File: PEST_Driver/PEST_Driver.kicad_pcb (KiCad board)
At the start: 2 copper layers, 68 x 53.2 mm, 148 parts, among them J1 Conn_01x02, J10 Conn_01x02, J11 Conn_01x02, J12 Conn_01x02, J13 Conn_01x02, J14 Conn_01x02, J15 Conn_01x02, J16 Conn_01x02, J17 Conn_01x02, J2 Conn_01x02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

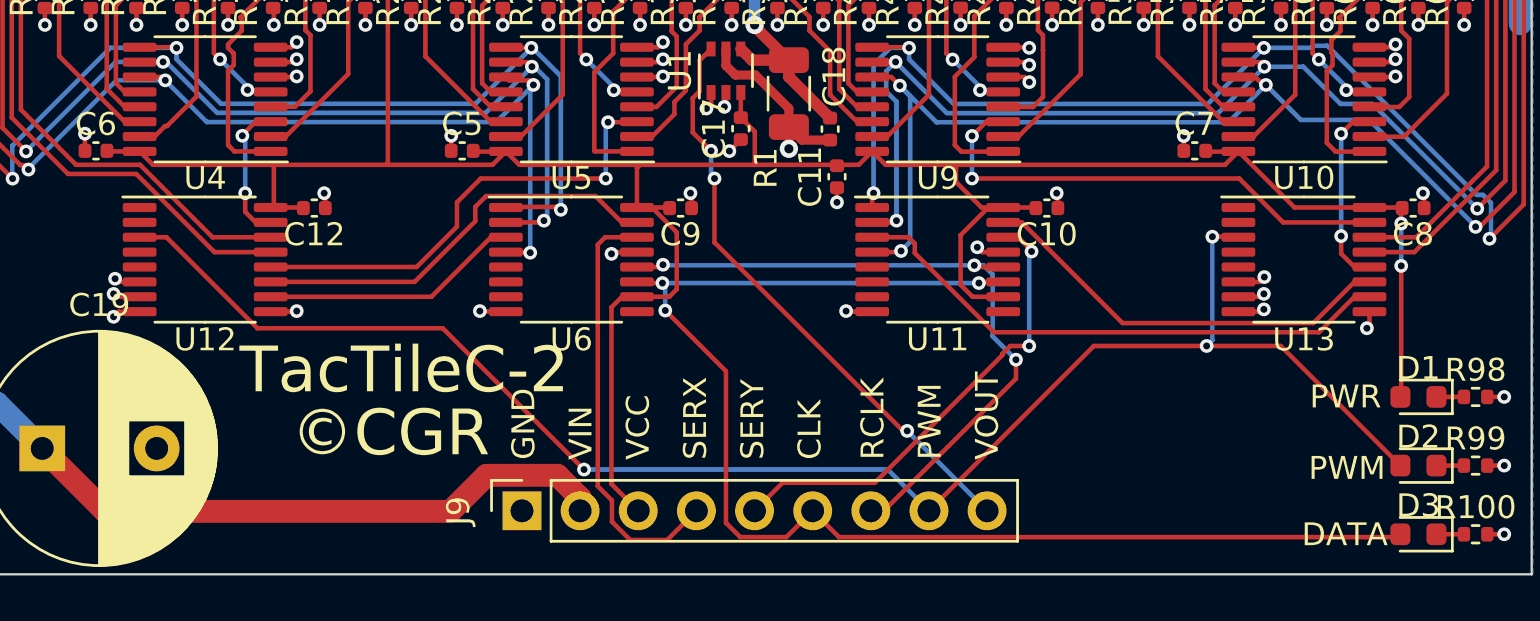
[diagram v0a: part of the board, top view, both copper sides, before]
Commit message: Finished wiring independent MOSFET and logic grounds
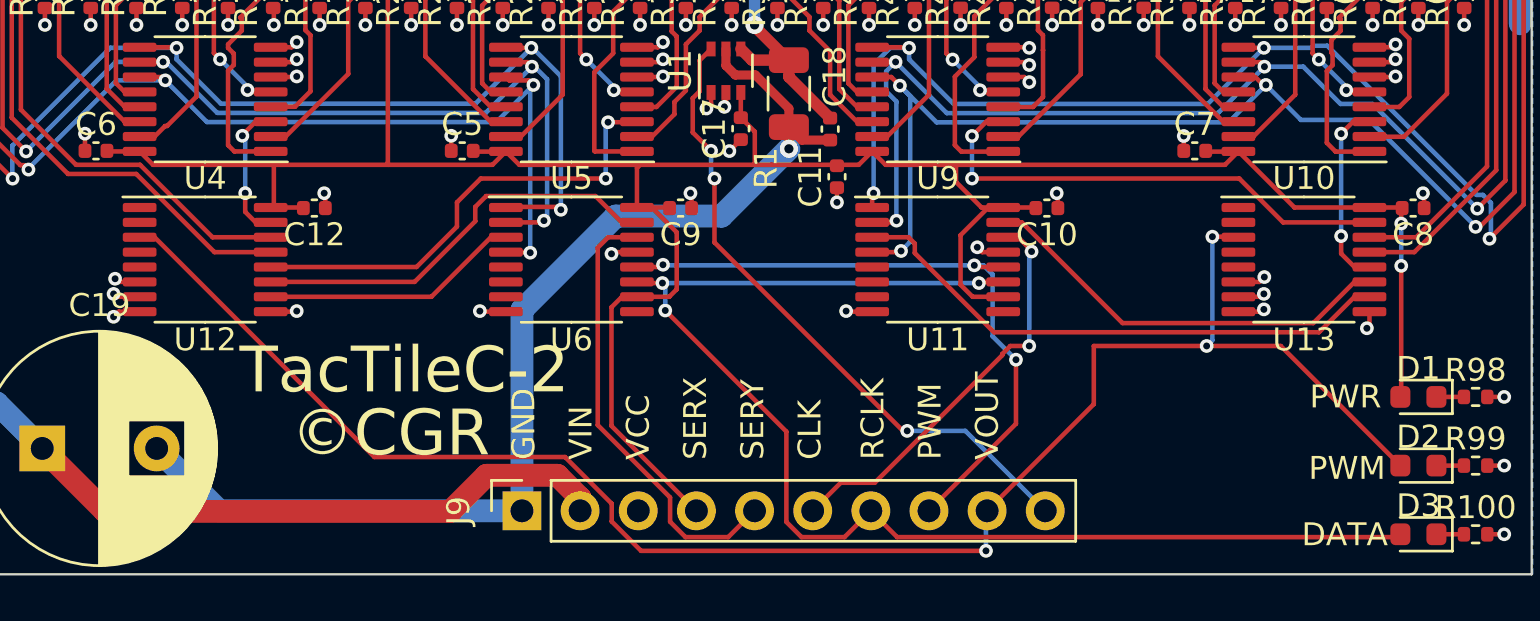
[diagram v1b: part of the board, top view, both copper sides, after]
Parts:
- J9: value Conn_01x09 -> Conn_01x10; footprint Connector_PinSocket_2.54mm:PinSocket_1x09_P2.54mm_Vertical -> Connector_PinSocket_2.54mm:PinSocket_1x10_P2.54mm_Vertical
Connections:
- C1 pad 1: GND -> GNDS
- C10 pad 1: GND -> GNDS
- C11 pad 1: GND -> GNDS
- C12 pad 1: GND -> GNDS
- C17 pad 1: GND -> GNDS
- C2 pad 1: GND -> GNDS
- C3 pad 1: GND -> GNDS
- C4 pad 1: GND -> GNDS
- C5 pad 1: GND -> GNDS
- C6 pad 1: GND -> GNDS
- C7 pad 1: GND -> GNDS
- C8 pad 1: GND -> GNDS
- C9 pad 1: GND -> GNDS
- J9 pad 3: VCC -> GNDS
- J9 pad 4: SERX -> VCC
- J9 pad 5: SERY -> SERX
- J9 pad 6: CLK -> SERY
- J9 pad 7: RCLK -> CLK
- J9 pad 8: PWM -> RCLK
- J9 pad 9: VOUT -> PWM
- R10 pad 1: GND -> GNDS
- R100 pad 2: GND -> GNDS
- R11 pad 2: GND -> GNDS
- R12 pad 1: GND -> GNDS
- R13 pad 2: GND -> GNDS
- R14 pad 1: GND -> GNDS
- R15 pad 2: GND -> GNDS
- R16 pad 1: GND -> GNDS
- R17 pad 2: GND -> GNDS
- R18 pad 1: GND -> GNDS
- R19 pad 2: GND -> GNDS
- R2 pad 1: GND -> GNDS
- R20 pad 1: GND -> GNDS
- R21 pad 2: GND -> GNDS
- R22 pad 1: GND -> GNDS
- R23 pad 2: GND -> GNDS
- R24 pad 1: GND -> GNDS
- R25 pad 2: GND -> GNDS
- R26 pad 1: GND -> GNDS
- R27 pad 2: GND -> GNDS
- R28 pad 1: GND -> GNDS
- R29 pad 2: GND -> GNDS
- R3 pad 2: GND -> GNDS
- R30 pad 1: GND -> GNDS
- R31 pad 2: GND -> GNDS
- R32 pad 1: GND -> GNDS
- R33 pad 2: GND -> GNDS
- R34 pad 1: GND -> GNDS
- R35 pad 2: GND -> GNDS
- R36 pad 1: GND -> GNDS
- R37 pad 2: GND -> GNDS
- R38 pad 1: GND -> GNDS
- R39 pad 2: GND -> GNDS
- R4 pad 1: GND -> GNDS
- R40 pad 1: GND -> GNDS
- R41 pad 2: GND -> GNDS
- R42 pad 1: GND -> GNDS
- R43 pad 2: GND -> GNDS
- R44 pad 1: GND -> GNDS
- R45 pad 2: GND -> GNDS
- R46 pad 1: GND -> GNDS
- R47 pad 2: GND -> GNDS
- R48 pad 1: GND -> GNDS
- R49 pad 2: GND -> GNDS
- R5 pad 2: GND -> GNDS
- R50 pad 1: GND -> GNDS
- R51 pad 2: GND -> GNDS
- R52 pad 1: GND -> GNDS
- R53 pad 2: GND -> GNDS
- R54 pad 1: GND -> GNDS
- R55 pad 2: GND -> GNDS
- R56 pad 1: GND -> GNDS
- R57 pad 2: GND -> GNDS
- R58 pad 1: GND -> GNDS
- R59 pad 2: GND -> GNDS
- R6 pad 1: GND -> GNDS
- R60 pad 1: GND -> GNDS
- R61 pad 2: GND -> GNDS
- R62 pad 1: GND -> GNDS
- R63 pad 2: GND -> GNDS
- R64 pad 1: GND -> GNDS
- R65 pad 2: GND -> GNDS
- R7 pad 2: GND -> GNDS
- R8 pad 1: GND -> GNDS
- R9 pad 2: GND -> GNDS
- R98 pad 2: GND -> GNDS
- R99 pad 2: GND -> GNDS
- U1 pad 1: GND -> GNDS
- U1 pad 2: GND -> GNDS
- U10 pad 6: GND -> GNDS
- U10 pad 7: GND -> GNDS
- U10 pad 8: GND -> GNDS
- U11 pad 13: GND -> GNDS
- U11 pad 8: GND -> GNDS
- U12 pad 6: GND -> GNDS
- U12 pad 7: GND -> GNDS
- U12 pad 8: GND -> GNDS
- U12 pad 9: GND -> GNDS
- U13 pad 6: GND -> GNDS
- U13 pad 7: GND -> GNDS
- U13 pad 8: GND -> GNDS
- U13 pad 9: GND -> GNDS
- U2 pad 6: GND -> GNDS
- U2 pad 7: GND -> GNDS
- U2 pad 8: GND -> GNDS
- U3 pad 6: GND -> GNDS
- U3 pad 7: GND -> GNDS
- U3 pad 8: GND -> GNDS
- U4 pad 6: GND -> GNDS
- U4 pad 7: GND -> GNDS
- U4 pad 8: GND -> GNDS
- U5 pad 6: GND -> GNDS
- U5 pad 7: GND -> GNDS
- U5 pad 8: GND -> GNDS
- U6 pad 13: GND -> GNDS
- U6 pad 8: GND -> GNDS
- U7 pad 6: GND -> GNDS
- U7 pad 7: GND -> GNDS
- U7 pad 8: GND -> GNDS
- U8 pad 6: GND -> GNDS
- U8 pad 7: GND -> GNDS
- U8 pad 8: GND -> GNDS
- U9 pad 6: GND -> GNDS
- U9 pad 7: GND -> GNDS
- U9 pad 8: GND -> GNDS
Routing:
- net GNDS: track 0.00 -> 124.6 mm, vias 0 -> 118
- net GND: track 132.7 -> 48.5 mm, vias 119 -> 1
- net PWM: track 71.2 -> 75.6 mm
- net VOUT: track 25.9 -> 28.5 mm
- net SERY: track 20.7 -> 18.2 mm
- net CLK: track 58.4 -> 56.8 mm
- net RCLK: track 30.8 -> 29.4 mm
- net VCC: track 195.2 -> 196.3 mm
- net SERX: track 18.8 -> 19.6 mm
- added copper zone on B.Cu, net GNDS
- removed copper zone on B.Cu, net GND

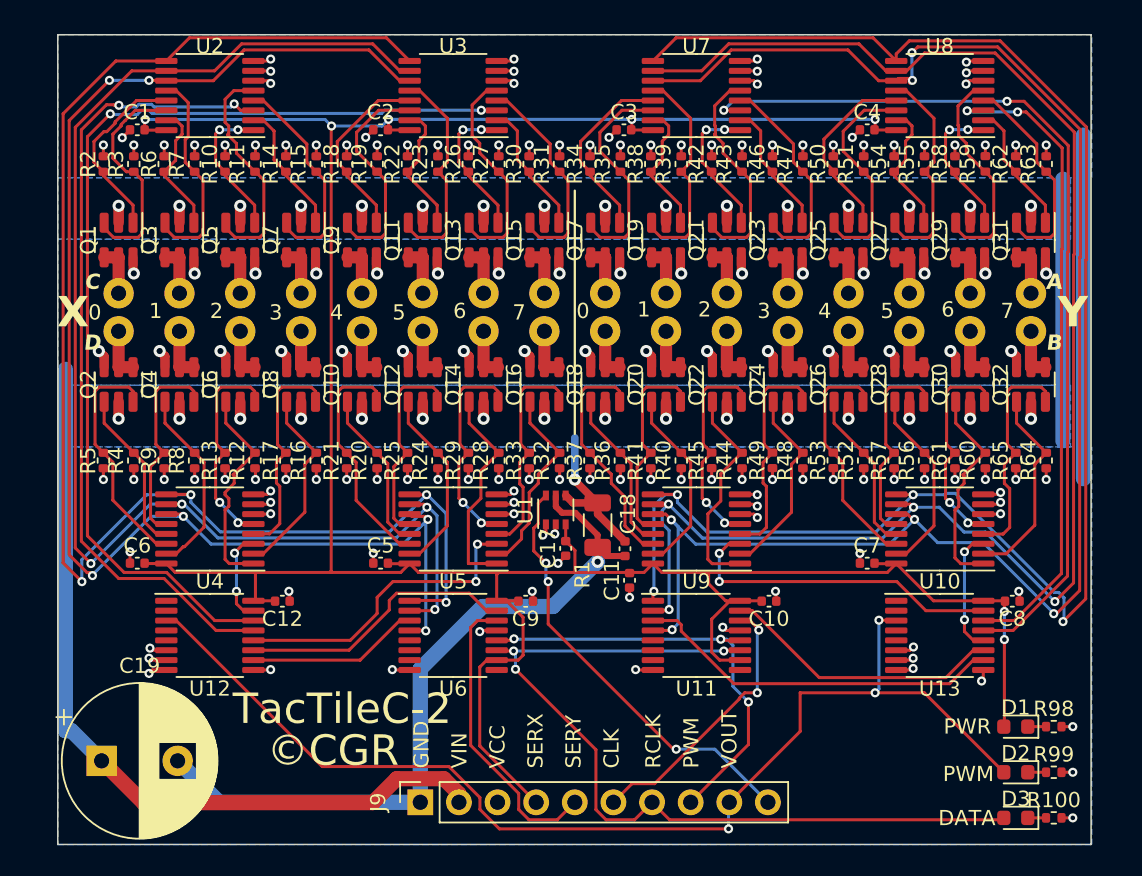
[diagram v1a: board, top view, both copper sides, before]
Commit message: Widened all power traces for more current support
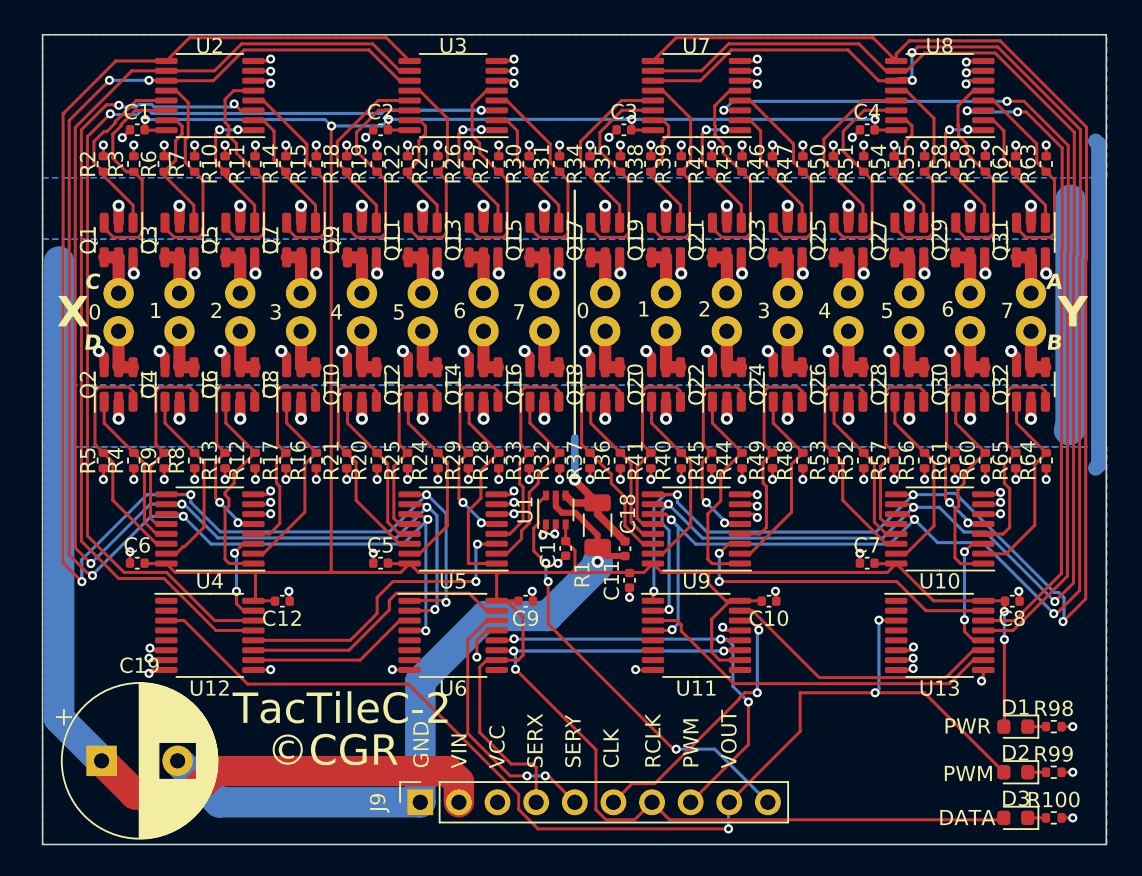
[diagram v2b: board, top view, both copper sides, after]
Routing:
- net VIN: track 89.9 -> 97.3 mm
- net SERX: track 19.6 -> 17.5 mm, vias 0 -> 2
- net SENSE: track 63.3 -> 61.3 mm
- net VCC: track 196.3 -> 197.1 mm
- net GNDS: track 124.6 -> 125.2 mm
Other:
- board size 68 x 53.2 mm -> 70 x 53.2 mm

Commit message: Added more pulldown resistors to PEST Driver
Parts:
- added G***: LOGO, Touchstone:logo, B.Cu at (53.8, 55.1)
- added R66: 10K, Resistor_SMD:R_0402_1005Metric, F.Cu at (66.5, 67.2)
- added R67: 10K, Resistor_SMD:R_0402_1005Metric, F.Cu at (34.8, 59.2)
- added R68: 10K, Resistor_SMD:R_0402_1005Metric, F.Cu at (37.9, 59.2)
- added R69: 10K, Resistor_SMD:R_0402_1005Metric, F.Cu at (37.9, 57.2)
- added R70: 10K, Resistor_SMD:R_0402_1005Metric, F.Cu at (41.0, 56.5)
- added R71: 10K, Resistor_SMD:R_0402_1005Metric, F.Cu at (83.4, 59.2)
- added R72: 10K, Resistor_SMD:R_0402_1005Metric, F.Cu at (85.3, 53.7)
- added R73: 10K, Resistor_SMD:R_0402_1005Metric, F.Cu at (70.0, 56.5)
- added R74: 10K, Resistor_SMD:R_0402_1005Metric, F.Cu at (83.4, 60.9)
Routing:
- net GNDS: track 125.2 -> 131.5 mm, vias 118 -> 127
- net Net-(U12-A1): track 67.3 -> 72.2 mm
- net Net-(U12-A2): track 6.19 -> 11.0 mm
- net Net-(U10-A): track 8.17 -> 10.6 mm
- net Net-(U12-A0): track 53.3 -> 54.7 mm
- net PWM: track 75.7 -> 74.4 mm
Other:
- board text added: "10"
- board text added: "11"
- board text added: "12"
- board text added: "13"
- board text added: "14"
- board text added: "15"
- board text added: "8"
- board text added: "9"
- board text added: "PEST Driver 1.1"
- board text removed: "A"
- board text removed: "B"
- board text removed: "C"
- board text removed: "D"
- board text removed: "TacTileC-2"

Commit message: Created basic DRIFT bus schematic and fixed PEST driver numbering
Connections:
- U10 pad 10: /Y_Control/S0 -> /Y_Control/S1
- U10 pad 9: /Y_Control/S1 -> /Y_Control/S2
- U11 pad 1: /Y_Control/S1 -> /Y_Control/S2
- U11 pad 15: /Y_Control/S2 -> /Y_Control/S3
- U11 pad 2: /Y_Control/S0 -> /Y_Control/S1
- U11 pad 3: /Y_Control/PHA -> /Y_Control/S0
- U12 pad 10: /X_Control/PHA -> /X_Control/S0
- U12 pad 11: /X_Control/S2 -> /X_Control/S3
- U13 pad 10: /Y_Control/PHA -> /Y_Control/S0
- U13 pad 11: /Y_Control/S2 -> /Y_Control/S3
- U2 pad 10: /X_Control/S0 -> /X_Control/S1
- U2 pad 9: /X_Control/S1 -> /X_Control/S2
- U3 pad 10: /X_Control/S0 -> /X_Control/S1
- U3 pad 9: /X_Control/S1 -> /X_Control/S2
- U4 pad 10: /X_Control/S0 -> /X_Control/S1
- U4 pad 9: /X_Control/S1 -> /X_Control/S2
- U5 pad 10: /X_Control/S0 -> /X_Control/S1
- U5 pad 9: /X_Control/S1 -> /X_Control/S2
- U6 pad 1: /X_Control/S1 -> /X_Control/S2
- U6 pad 15: /X_Control/S2 -> /X_Control/S3
- U6 pad 2: /X_Control/S0 -> /X_Control/S1
- U6 pad 3: /X_Control/PHA -> /X_Control/S0
- U7 pad 10: /Y_Control/S0 -> /Y_Control/S1
- U7 pad 9: /Y_Control/S1 -> /Y_Control/S2
- U8 pad 10: /Y_Control/S0 -> /Y_Control/S1
- U8 pad 9: /Y_Control/S1 -> /Y_Control/S2
- U9 pad 10: /Y_Control/S0 -> /Y_Control/S1
- U9 pad 9: /Y_Control/S1 -> /Y_Control/S2
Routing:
- net /Y_Control/S2: track 18.6 -> 109.2 mm, vias 0 -> 4
- net /X_Control/S0: track 90.9 -> 11.4 mm, vias 4 -> 0
- net /X_Control/S2: track 18.4 -> 97.8 mm, vias 0 -> 4
- net /Y_Control/S0: track 103.6 -> 24.3 mm, vias 4 -> 0
- net /Y_Control/PHA: track 24.3 -> 0.00 mm
- net /Y_Control/S3: track 0.00 -> 18.6 mm
- net /X_Control/S3: track 0.00 -> 18.4 mm
- net /X_Control/PHA: track 11.4 -> 0.00 mm
- net /X_Control/S1: track 97.8 -> 90.9 mm
- net /Y_Control/S1: track 109.2 -> 103.6 mm

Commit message: Fixed some silkscreen stuff, started DRIFT bus layout
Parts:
- R100, R98, R99: value 500 -> 1.2K
- moved R66 2.70 mm to (69.2, 67.2)
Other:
- board text added: "5V"
- board text added: "SENSE"
- board text added: "SGND"
- board text removed: "VCC"
- board text removed: "VOUT"

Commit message: Finalized PCBs for fabrication
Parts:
- removed G***: LOGO, Touchstone:logo
- added REF**: Mounting_Hole, Touchstone:Mounting_Hole, F.Cu at (21.0, 22.8)
- added REF**: Mounting_Hole, Touchstone:Mounting_Hole, F.Cu at (70.0, 23.0)
- added REF**: Mounting_Hole, Touchstone:Mounting_Hole, F.Cu at (86.5, 22.8)
- added REF**: Mounting_Hole, Touchstone:Mounting_Hole, F.Cu at (38.0, 23.0)
- moved C1 0.15 mm to (25.2, 26.4)
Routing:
- net /X_Control/DIR: track 91.9 -> 93.4 mm
- net Net-(U12-A0): track 54.7 -> 56.1 mm
- net Net-(U12-A1): track 72.2 -> 73.5 mm
- net /Y_Control/S1: track 103.6 -> 104.2 mm
- net /Y_Control/DIR: track 107.7 -> 108.4 mm
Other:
- board size 70 x 53.2 mm -> 71 x 53.2 mm
